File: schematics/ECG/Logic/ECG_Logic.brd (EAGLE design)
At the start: 30.1 x 26.7 mm, 78 parts, among them IC1 ADS1293, IC10 FSA4157, IC2 LIS3DH, IC3 MCP1703, IC4 CC2541, IC5 FSA4157, IC6 FSA4157, IC7 FSA4157, IC9 LTC6907, X1 XTAL-2SMD, X2 XTAL_403

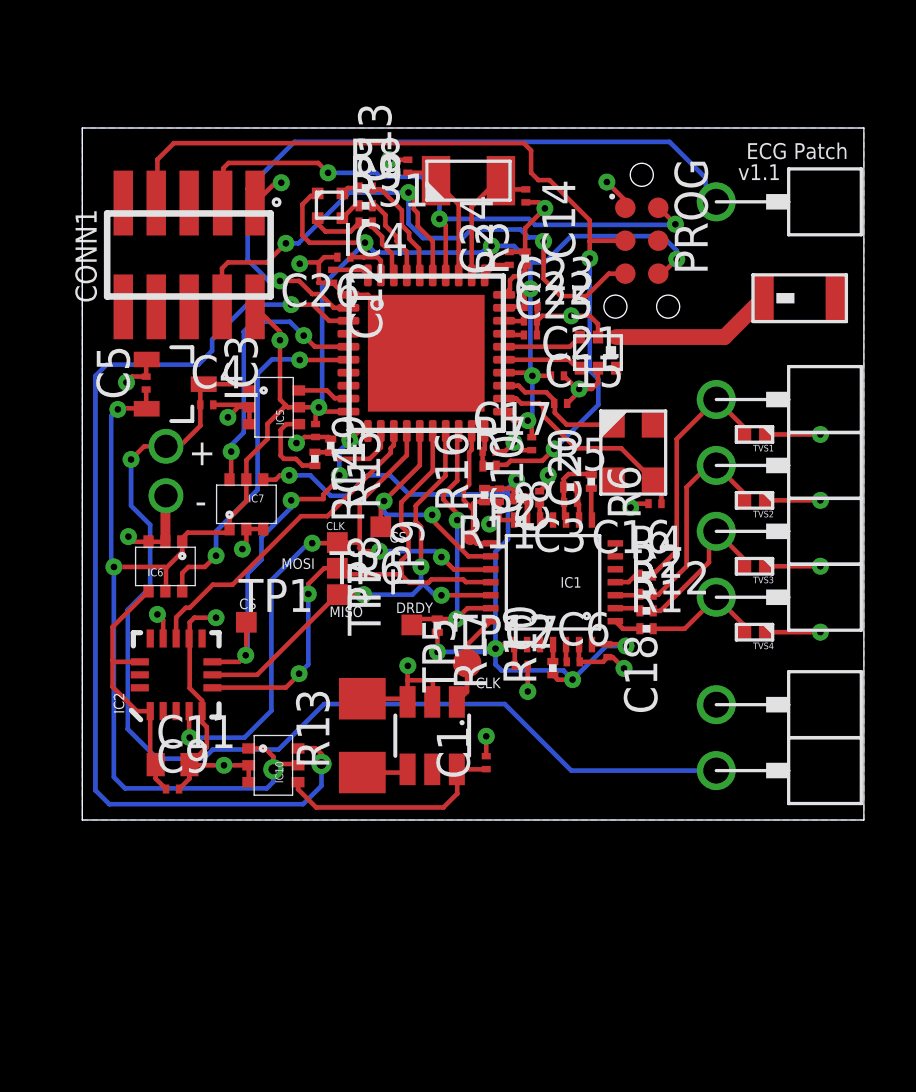
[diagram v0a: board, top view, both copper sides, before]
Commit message: redesigned patch board and charging board
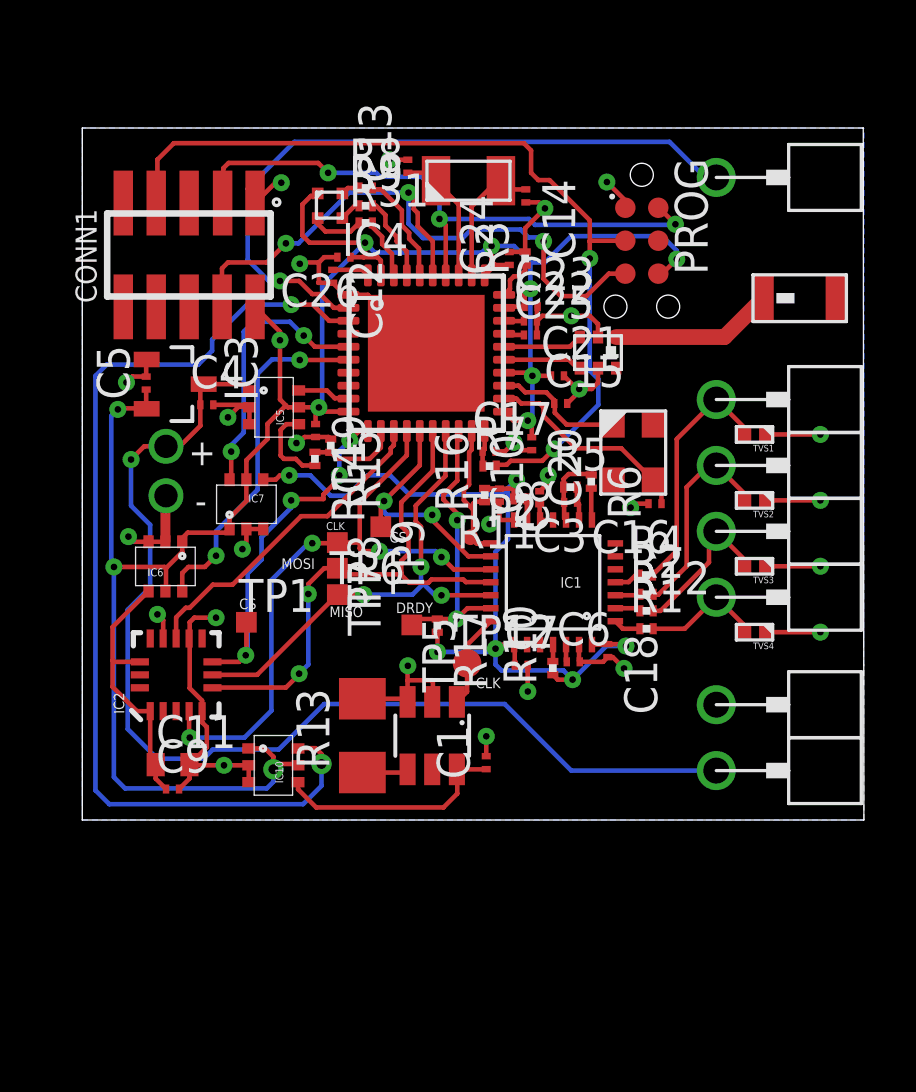
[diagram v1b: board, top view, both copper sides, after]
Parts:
- moved U$7 0.94 mm to (24.4, 24.8)
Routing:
- net BOARD_DETECT: track 27.5 -> 26.8 mm
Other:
- board text removed: "ECG Patch"
- board text removed: "v1.1"
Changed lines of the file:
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@@
 <plain>
 <wire x1="0" y1="0" x2="30.1244" y2="0" width="0" layer="20"/>
-<wire x1="30.1244" y1="0" x2="30.1244" y2="26.67" width="0" layer="20"/>
-<wire x1="30.1244" y1="26.67" x2="0" y2="26.67" width="0" layer="20"/>
+<wire x1="30.1244" y1="0" x2="30.099" y2="26.67" width="0" layer="20"/>
+<wire x1="30.099" y1="26.67" x2="0" y2="26.67" width="0" layer="20"/>
 <wire x1="0" y1="26.67" x2="0" y2="0" width="0" layer="20"/>
-<text x="29.5148" y="26.0858" size="0.6096" layer="21" rot="R180">ECG Patch</text>
-<text x="25.273" y="24.6634" size="0.6096" layer="21">v1.1</text>
 <text x="9.525" y="7.8232" size="0.4064" layer="21">MISO</text>
 <text x="7.6708" y="9.6774" size="0.4064" layer="21">MOSI</text>
@@
 <element name="U$6" library="pins" package="TARGET_RA" value="TARGET_RA" x="24.4348" y="1.905"/>
 <element name="IC10" library="fairchild" package="SC70-6" value="FSA4157" x="7.366" y="2.0574" rot="R270"/>
-<element name="U$7" library="pins" package="TARGET_RA" value="TARGET_RA" x="24.4348" y="23.8252"/>
+<element name="U$7" library="pins" package="TARGET_RA" value="TARGET_RA" x="24.4348" y="24.765"/>
 </elements>
 <signals>
@@
 <wire x1="6.3754" y1="24.3332" x2="8.1788" y2="26.1366" width="0.1778" layer="16"/>
 <wire x1="8.1788" y1="26.1366" x2="22.6314" y2="26.1366" width="0.1778" layer="16"/>
-<wire x1="22.6314" y1="26.1366" x2="24.0284" y2="24.7396" width="0.1778" layer="16"/>
-<wire x1="24.0284" y1="24.7396" x2="24.0284" y2="24.2316" width="0.1778" layer="16"/>
-<wire x1="24.0284" y1="24.2316" x2="24.4348" y2="23.8252" width="0.1778" layer="16"/>
+<wire x1="24.4348" y1="24.765" x2="24.003" y2="24.765" width="0.1778" layer="16"/>
+<wire x1="24.003" y1="24.765" x2="22.6314" y2="26.1366" width="0.1778" layer="16"/>
 </signal>
 </signals>

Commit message: added new low profile 4Mhz xtal
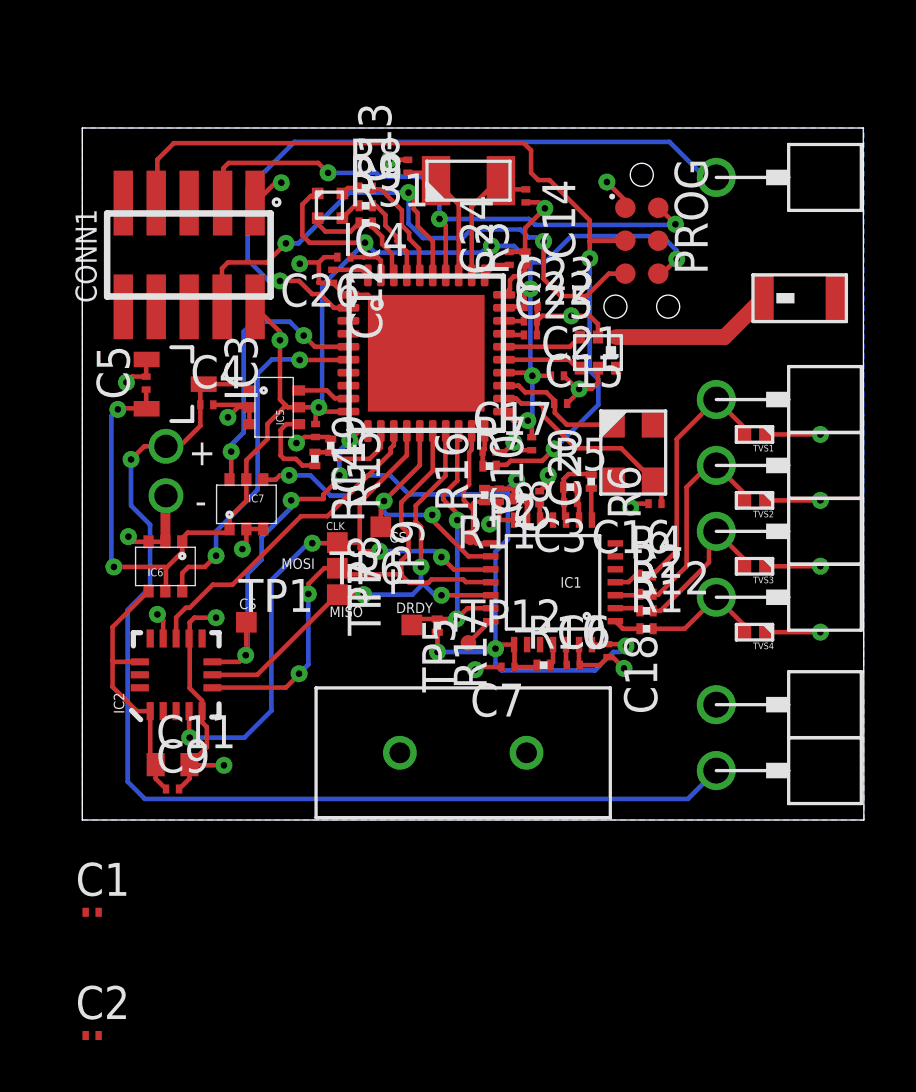
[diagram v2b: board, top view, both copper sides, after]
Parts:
- removed IC10: FSA4157, fairchild:SC70-6
- removed IC9: LTC6907, linear:TSOT23-6
- removed R13: 500K, rcl:R1206
- added C2: 20pF, rcl:C0201
- added X3: ECS-40-20-4VX, ecs:ECS-40-20-4VX
- C1: value 0.1uF -> 20pF
- TP12: value TPSTP11R -> TPSTP06R; device testpad:TP11R -> testpad:TP06R
- moved C1 16.2 mm to (0.38, -3.56), turned to 0 degrees
- moved TP12 0.79 mm to (14.9, 6.83)
- moved C7 0.51 mm to (16.4, 5.89), turned to 180 degrees
- moved R10 0.37 mm to (17.8, 5.97), turned to 0 degrees
- moved C6 0.13 mm to (18.9, 5.97)
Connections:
- removed net GRD: IC9.5
- removed net N$14: IC9.4, R13.1
- removed net OSC_VCC: C1.1, IC10.4, IC9.6
- new net N$1: C1.1, X3.1
- new net N$10: C1.2
- new net N$2: C2.1, X3.2
- new net N$7: C2.2
- net CLK: no longer IC9.1
- net GND: no longer C1.2, IC10.2, IC10.3, IC9.2, IC9.3, R13.2
- net OSC_SW_VCC: no longer IC10.6
- net VCC: no longer IC10.1, IC10.5
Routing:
- net OSC_SW_VCC: track 38.8 -> 0.00 mm, vias 2 -> 0
- net VCC: track 89.8 -> 72.0 mm, vias 11 -> 10
- net OSC_VCC: track 9.00 -> 0.00 mm
- net GND: track 68.1 -> 60.9 mm, vias 28 -> 26
- net CLK: track 3.68 -> 1.21 mm
- net N$14: track 2.04 -> 0.00 mm
- net ECG_VCC: track 33.0 -> 32.9 mm, vias 6 -> 5

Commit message: expanded board size for new low profile crystal. Moved ecg input targets for shorter trace lengths to ADS1293
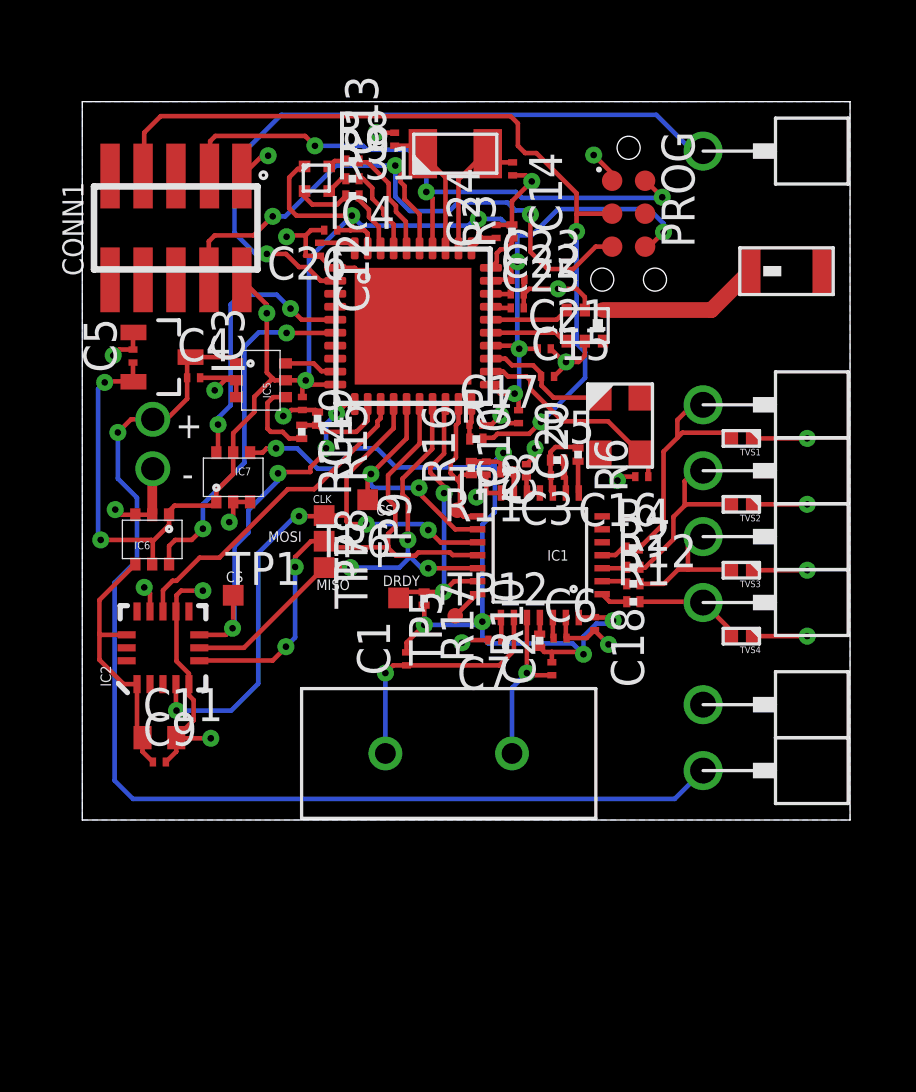
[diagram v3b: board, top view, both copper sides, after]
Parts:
- moved C2 22.7 mm to (18.1, 5.83), turned to 90 degrees
- moved C1 15.6 mm to (12.5, 6.21), turned to 90 degrees
- moved C21 1.16 mm to (17.8, 18.2)
- moved R9 1.16 mm to (10.4, 24.7)
- moved C12 1.16 mm to (9.14, 22.0)
- moved C22 1.16 mm to (16.8, 20.3)
- moved C24 1.16 mm to (16.0, 22.7)
- moved IC1 1.16 mm to (17.6, 10.2)
- moved IC4 1.16 mm to (12.7, 19.0)
- moved PROG 1.16 mm to (21.1, 25.9)
- moved R3 1.16 mm to (16.6, 22.7)
- moved C19 1.16 mm to (8.48, 16.1)
- moved R7 1.16 mm to (15.2, 14.7)
- moved C20 1.16 mm to (16.8, 15.5)
- moved R15 1.16 mm to (9.07, 15.5)
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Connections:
- removed net N$1: C1.1, X3.1
- removed net N$10: C1.2
- removed net N$2: C2.1, X3.2
- removed net N$7: C2.2
- new net XTAL1: C1.1, IC1.23, X3.1
- new net XTAL2: C2.1, IC1.24, X3.2
- net ECG_VCC: now also C1.2, C2.2
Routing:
- net XTAL1: track 0.00 -> 9.69 mm, vias 0 -> 1
- net XTAL2: track 0.00 -> 6.48 mm, vias 0 -> 1
- net ECG_VCC: track 32.9 -> 36.3 mm, vias 5 -> 6
- net LL: track 8.08 -> 6.85 mm
- net BATT: track 43.2 -> 44.2 mm
- net LA: track 6.03 -> 5.48 mm
- net RA: track 4.73 -> 4.19 mm
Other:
- board size 30.1 x 26.7 mm -> 29.6 x 27.7 mm
- board text removed: "Added LTC6907 , C1, and R13 (PNM0603E5002BST5)"
- board text removed: "removed X3,C1,C2"
- board text removed: "review/fix LEDs?"

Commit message: updated all boards to slightly larger dimensions and new target/piston positions
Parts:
- renumbered U$1 to P1, U$2 to P2, U$3 to P3, U$4 to P4, U$5 to P5, U$6 to P6, U$7 to P7
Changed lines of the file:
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@@
 <attribute name="TP_SIGNAL_NAME" value="" x="14.4526" y="11.938" size="1.778" layer="27" display="off"/>
 </element>
-<element name="U$1" library="pins" package="TARGET_RA" value="TARGET_RA" x="23.9268" y="13.462"/>
-<element name="U$2" library="pins" package="TARGET_RA" value="TARGET_RA" x="23.9268" y="10.922"/>
-<element name="U$3" library="pins" package="TARGET_RA" value="TARGET_RA" x="23.9268" y="8.382"/>
-<element name="U$4" library="pins" package="TARGET_RA" value="TARGET_RA" x="23.9268" y="16.002"/>
-<element name="U$5" library="pins" package="TARGET_RA" value="TARGET_RA" x="23.9268" y="4.445"/>
-<element name="U$6" library="pins" package="TARGET_RA" value="TARGET_RA" x="23.9268" y="1.905"/>
-<element name="U$7" library="pins" package="TARGET_RA" value="TARGET_RA" x="23.9268" y="25.781"/>
+<element name="P1" library="pins" package="TARGET_RA" value="TARGET_RA" x="23.9268" y="13.462"/>
+<element name="P2" library="pins" package="TARGET_RA" value="TARGET_RA" x="23.9268" y="10.922"/>
+<element name="P3" library="pins" package="TARGET_RA" value="TARGET_RA" x="23.9268" y="8.382"/>
+<element name="P4" library="pins" package="TARGET_RA" value="TARGET_RA" x="23.9268" y="16.002"/>
+<element name="P5" library="pins" package="TARGET_RA" value="TARGET_RA" x="23.9268" y="4.445"/>
+<element name="P6" library="pins" package="TARGET_RA" value="TARGET_RA" x="23.9268" y="1.905"/>
+<element name="P7" library="pins" package="TARGET_RA" value="TARGET_RA" x="23.9268" y="25.781"/>
 <element name="X3" library="ecs" package="ECS-40-20-4VX" value="ECS-40-20-4VX" x="14.1224" y="2.5654"/>
 <element name="C1" library="rcl" package="C0201" value="20pF" x="12.4968" y="6.2103" rot="R90"/>
@@
 <wire x1="8.9886" y1="15.8028" x2="9.0678" y2="15.7236" width="0.1778" layer="1"/>
 <wire x1="8.4836" y1="15.8028" x2="8.0558" y2="15.8028" width="0.1778" layer="1"/>
-<contactref element="U$5" pad="1"/>
+<contactref element="P5" pad="1"/>
 <via x="27.94" y="14.7066" extent="1-16" drill="0.254"/>
 <via x="2.7178" y="13.5382" extent="1-16" drill="0.9"/>
@@
 <contactref element="R1" pad="2"/>
 <contactref element="TVS4" pad="2"/>
-<contactref element="U$3" pad="1"/>
+<contactref element="P3" pad="1"/>
 <wire x1="21.494" y1="8.4126" x2="23.8962" y2="8.4126" width="0.1778" layer="1"/>
 <wire x1="23.8962" y1="8.4126" x2="23.9268" y2="8.382" width="0.1778" layer="1"/>
@@
 <contactref element="R2" pad="2"/>
 <contactref element="TVS2" pad="2"/>
-<contactref element="U$1" pad="1"/>
+<contactref element="P1" pad="1"/>
 <wire x1="21.5068" y1="9.7282" x2="21.494" y2="9.741" width="0.1778" layer="1"/>
 <wire x1="21.6916" y1="9.7282" x2="22.7838" y2="10.8204" width="0.1778" layer="1"/>
@@
 <contactref element="R4" pad="2"/>
 <contactref element="TVS1" pad="2"/>
-<contactref element="U$4" pad="1"/>
+<contactref element="P4" pad="1"/>
 <wire x1="22.4028" y1="11.4156" x2="21.4686" y2="10.4814" width="0.1778" layer="1"/>
 <wire x1="25.0008" y1="14.7066" x2="25.0008" y2="14.928" width="0.1778" layer="1"/>
@@
 <contactref element="R12" pad="2"/>
 <contactref element="TVS3" pad="2"/>
-<contactref element="U$2" pad="1"/>
+<contactref element="P2" pad="1"/>
 <wire x1="21.494" y1="9.1022" x2="22.4118" y2="9.1022" width="0.1778" layer="1"/>
 <wire x1="22.4118" y1="9.1022" x2="22.9616" y2="9.652" width="0.1778" layer="1"/>
@@
 <wire x1="4.0426" y1="17.0434" x2="4.0426" y2="16.2346" width="0.1778" layer="1"/>
 <via x="1.3716" y="14.9352" extent="1-16" drill="0.254"/>
-<contactref element="U$6" pad="1"/>
+<contactref element="P6" pad="1"/>
 <wire x1="1.3716" y1="14.9352" x2="1.3716" y2="13.1572" width="0.1778" layer="16"/>
 <wire x1="1.3716" y1="13.1572" x2="2.1082" y2="12.4206" width="0.1778" layer="16"/>
@@
 </signal>
 <signal name="BOARD_DETECT">
-<contactref element="U$7" pad="1"/>
+<contactref element="P7" pad="1"/>
 <contactref element="IC4" pad="2"/>
 <wire x1="9.7498" y1="20.7814" x2="9.1906" y2="20.7814" width="0.1778" layer="1"/>
